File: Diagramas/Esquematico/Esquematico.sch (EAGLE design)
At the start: 42 parts, among them IC1 RASPBERRY_PI_ZERO_W_(V1.3), IC2 3071, K1 SRD-05VDC-SL-C, K2 SRD-05VDC-SL-C, K3 SRD-05VDC-SL-C, K4 SRD-05VDC-SL-C, K5 SRD-05VDC-SL-C

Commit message: modulo gsm
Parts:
- removed SV1, SV2: (no value), con-lsta:FE08W
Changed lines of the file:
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@@
 <setting verticaltext="up"/>
 </settings>
-<grid distance="0.1" unitdist="inch" unit="mm" style="dots" multiple="1" display="yes" altdistance="0.01" altunitdist="inch" altunit="mm"/>
+<grid distance="0.5" unitdist="mm" unit="mm" style="dots" multiple="1" display="yes" altdistance="0.01" altunitdist="inch" altunit="mm"/>
 <layers>
 <layer number="1" name="Top" color="4" fill="1" visible="no" active="no"/>
@@
 <part name="IC2" library="3071" deviceset="3071" device=""/>
 <part name="X6" library="con-wago-508" library_urn="urn:adsk.eagle:library:196" deviceset="W232-3" device="" package3d_urn="urn:adsk.eagle:package:10743/1"/>
-<part name="SV1" library="con-lsta" library_urn="urn:adsk.eagle:library:161" deviceset="FE08W" device="" package3d_urn="urn:adsk.eagle:package:8197/1"/>
-<part name="SV2" library="con-lsta" library_urn="urn:adsk.eagle:library:161" deviceset="FE08W" device="" package3d_urn="urn:adsk.eagle:package:8197/1"/>
 </parts>
 <sheets>
@@
 <attribute name="NAME" x="-75.565" y="173.609" size="1.778" layer="95" rot="R180"/>
 </instance>
-<instance part="SV1" gate="G$1" x="170.18" y="63.5" smashed="yes">
-<attribute name="VALUE" x="168.91" y="50.8" size="1.778" layer="96"/>
-<attribute name="NAME" x="168.91" y="76.962" size="1.778" layer="95"/>
-</instance>
-<instance part="SV2" gate="G$1" x="200.66" y="63.5" smashed="yes" rot="MR0">
-<attribute name="VALUE" x="201.93" y="50.8" size="1.778" layer="96" rot="MR0"/>
-<attribute name="NAME" x="201.93" y="76.962" size="1.778" layer="95" rot="MR0"/>
-</instance>
 </instances>

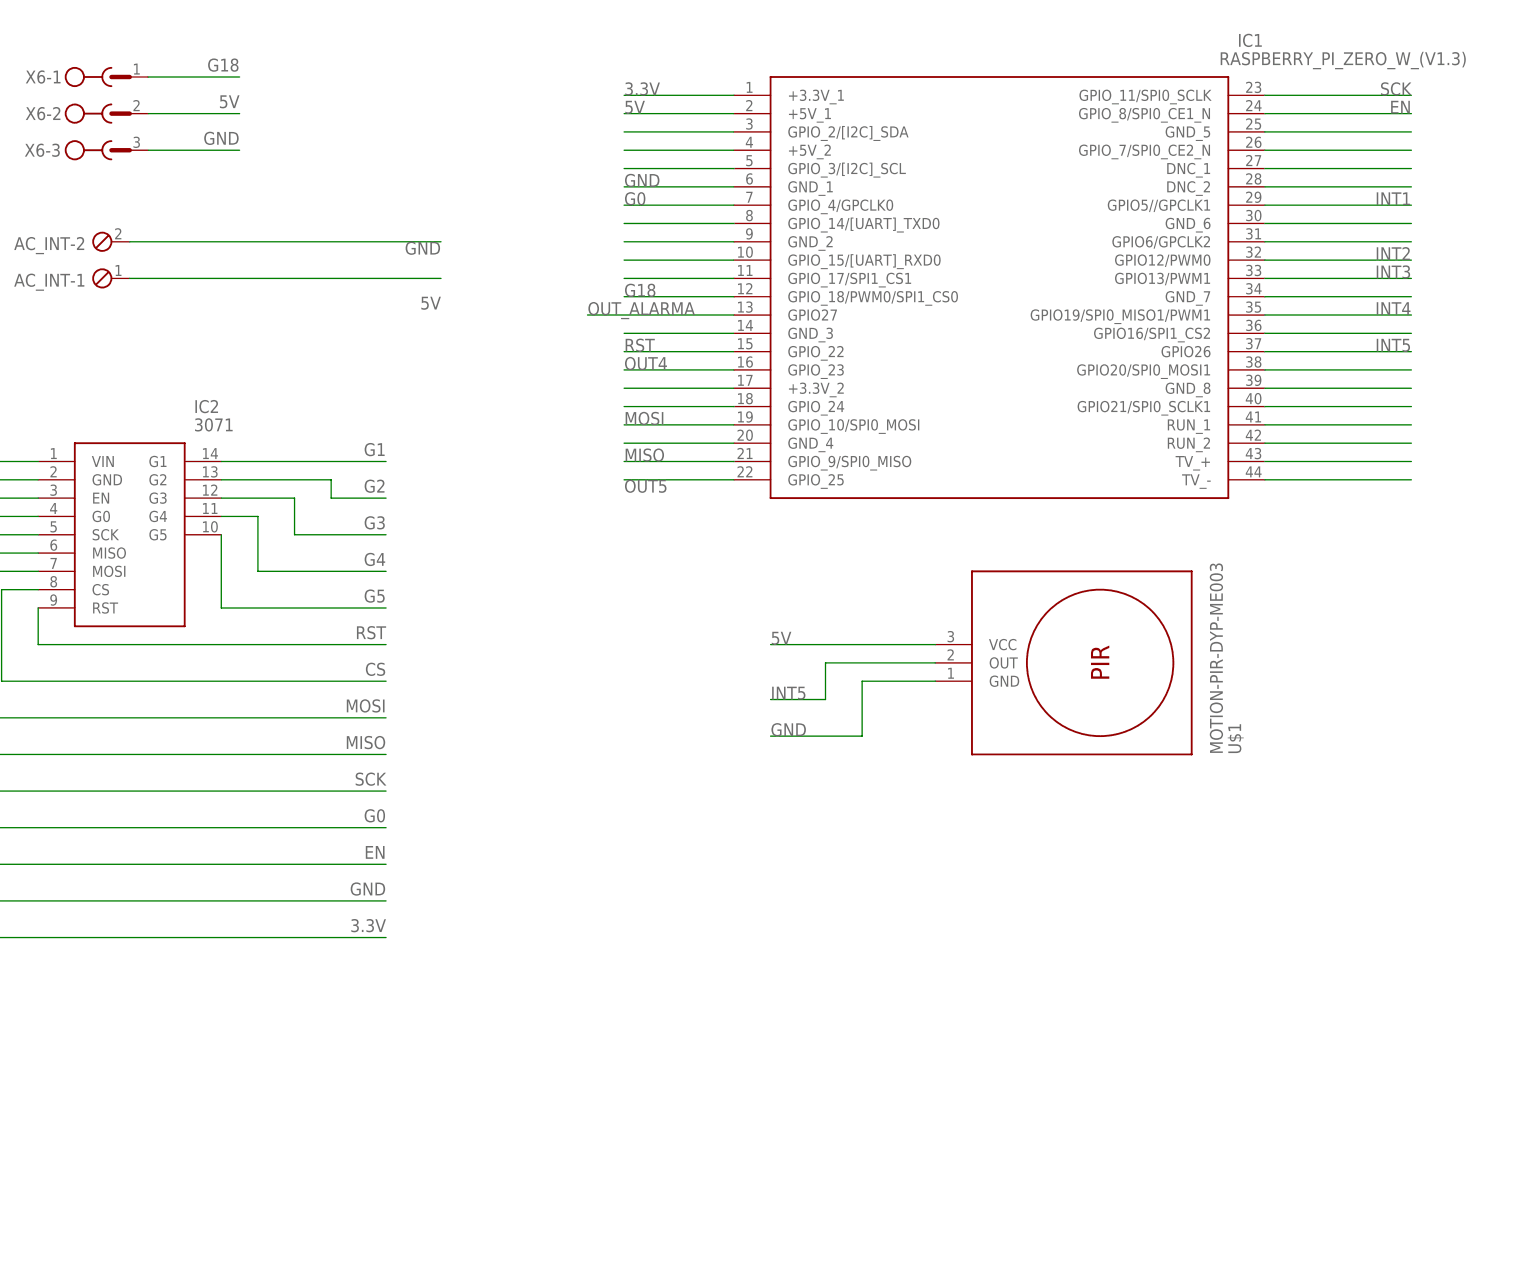
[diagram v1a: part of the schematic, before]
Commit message: cambio de lugar de lora
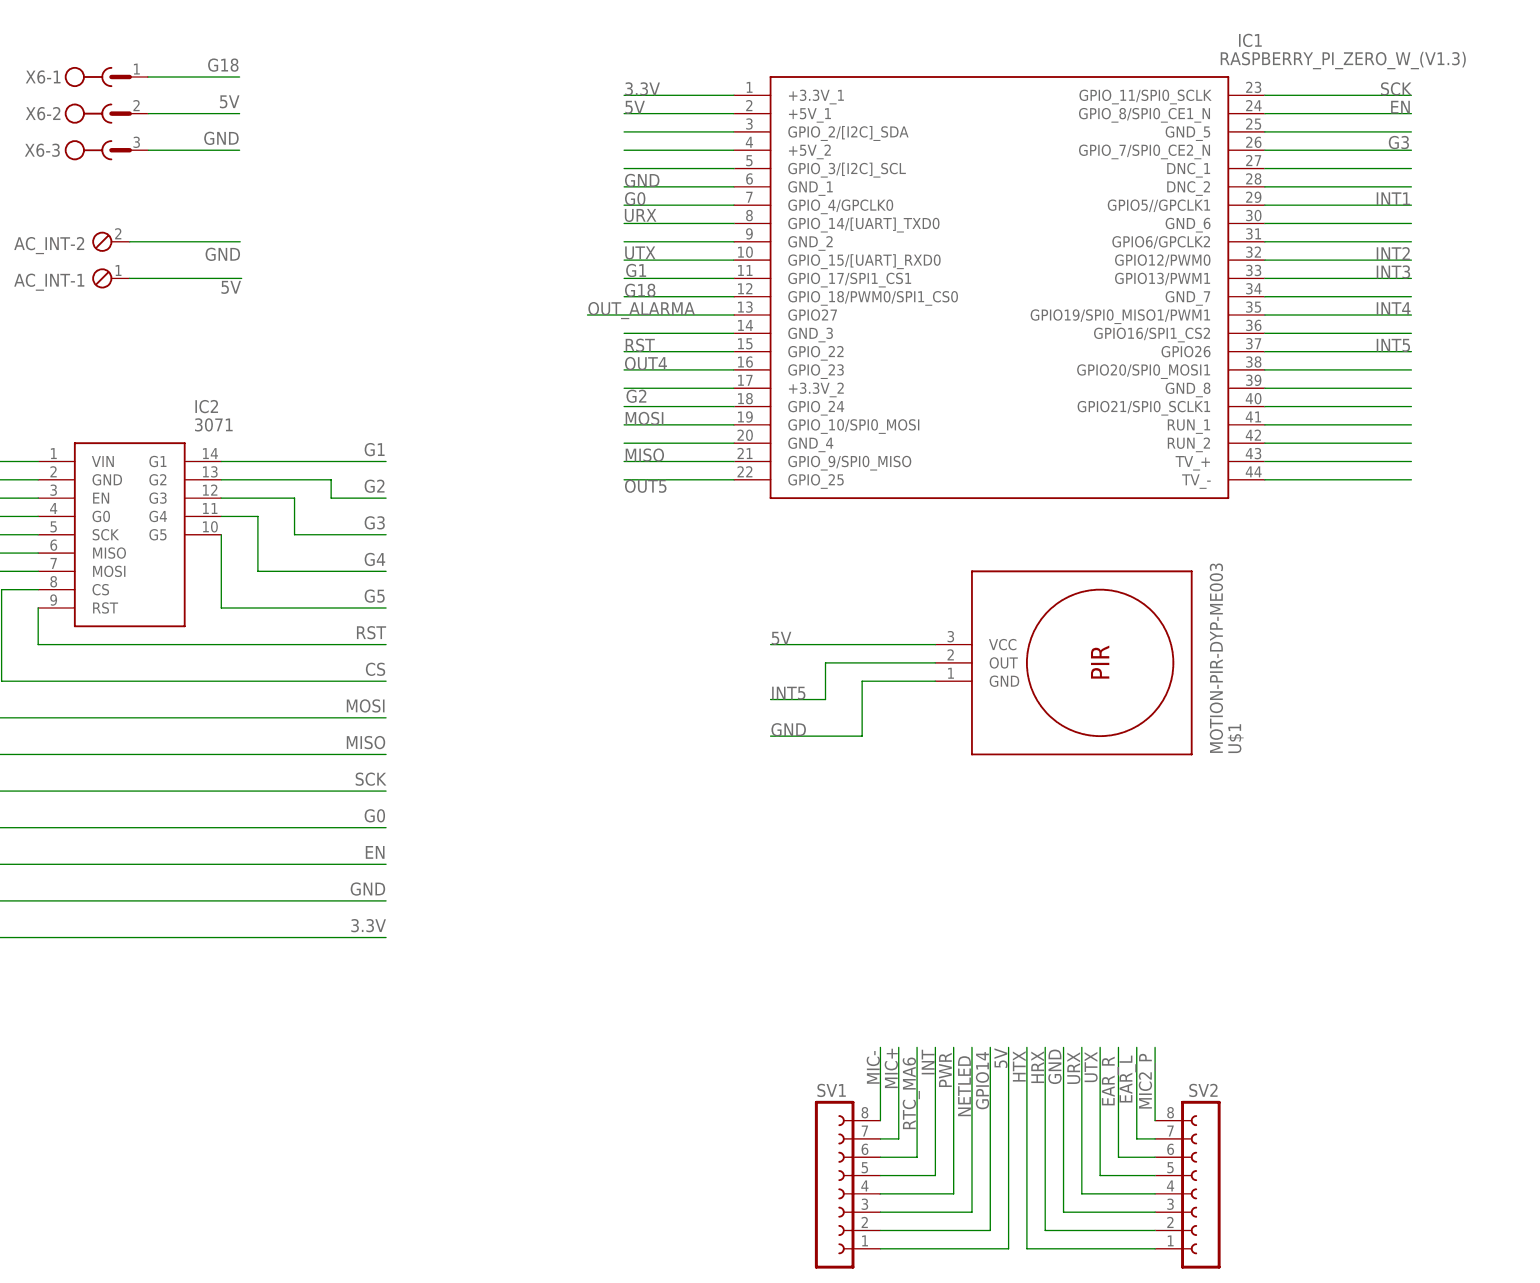
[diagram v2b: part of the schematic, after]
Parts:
- added SV1, SV2: (no value), con-lsta:FE08-1
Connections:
- removed net N$20: IC1.GPIO_17/SPI1_CS1
- removed net N$24: IC1.GPIO_24
- removed net N$31: IC1.GPIO_7/SPI0_CE2_N
- removed net N$6: IC1.GPIO_14/[UART]_TXD0
- removed net N$8: IC1.GPIO_15/[UART]_RXD0
- new net EAR_L: SV2.7
- new net EAR_R: SV2.6
- new net GPIO14: SV1.2
- new net HRX: SV2.2
- new net HTX: SV2.1
- new net INT: SV1.5
- new net MIC+: SV1.7
- new net MIC-: SV1.8
- new net MIC2_P: SV2.8
- new net NETLED: SV1.3
- new net PWR: SV1.4
- new net RTC_MA6: SV1.6
- new net URX: IC1.GPIO_14/[UART]_TXD0, SV2.4
- new net UTX: IC1.GPIO_15/[UART]_RXD0, SV2.5
- net 5V: now also SV1.1
- net G1: now also IC1.GPIO_17/SPI1_CS1
- net G2: now also IC1.GPIO_24
- net G3: now also IC1.GPIO_7/SPI0_CE2_N
- net GND: now also SV2.3
